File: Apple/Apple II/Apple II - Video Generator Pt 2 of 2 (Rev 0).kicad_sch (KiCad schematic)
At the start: 0 parts

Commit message: Finished Apple II - Sheet 17 - Video Generator Part 2 (Rev 0)
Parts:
- added B11: 74LS08, symbol Apple II:B11_74LS08
- added B12: 74LS11, symbol Apple II:B12_74LS11
- added B13: 74LS02, symbol Apple II:B13_74LS02
- added C11: 74LS04, symbol Apple II:C11_74LS04
- added C14: 74LS32, symbol Apple II:C14_74LS32
- added C2: 47pF, symbol Device:C_Small
- added C3: 5-50pF, symbol Device:C_Variable
- added J324: COMPOSITE VIDEO OUTPUT, symbol Connector:Conn_Coaxial
- added J432: AUX VIDEO CONNECTOR, symbol Connector:Conn_01x04_Male
- added L1: 27µH, symbol Device:L
- added Q?: 2N3904, Package_TO_SOT_THT:TO-92_Inline, symbol Transistor_BJT:2N3904
- added R10: 27Ω, symbol Device:R_US
- added R11: 200Ω, symbol Device:R_Potentiometer_US
- added R5: 1K, symbol Device:R_US
- added R6: 2.7K, symbol Device:R_US
- added R7: 1.5K, symbol Device:R_US
- added R8: 2K, symbol Device:R_US
- added U? (x2): C13_74LS51, symbol Apple II:C13_74LS51
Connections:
- new net: C2.1, C3.1, L1.1, R5.2, R6.1
- new net: Q?.2 (B), R6.2, R7.2, R8.2
- new net: C11.4, U?.1
- new net: B11.8, C14.4, U?.13
- new net: B12.1, B13.1
- new net: J324.1 (In), R10.2
- new net: J432.2 (Pin_2), Q?.1 (E), R11.1
- new net: R10.1, R11.2
- new net +12V: J432.4 (Pin_4)
- new net -5V: J432.3 (Pin_3)
- new net BLANKING: C14.6
- new net COLOR_BURST: B12.12, R5.1
- new net COLOR_REF_{35}: B13.2
- new net Earth: C2.2, C3.2, J324.2 (Ext), J432.1 (Pin_1), L1.2, R11.3
- new net H2: B13.3
- new net H3: U?.10, U?.11, U?.3
- new net H4: B12.2, U?.2
- new net H5: U?.4, U?.5
- new net HBL: B12.13, C14.5, U?.6, U?.9
- new net SYNC_{19}: R8.1, U?.8
- new net V1: C11.3
- new net V2: U?.12
- new net V3: B11.9
- new net V4: B11.10
- new net VIDEO_DATA: R7.1
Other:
- note added: "FROM CLOCK GENERATOR"
- note added: "FROM PART 1"
- note added: "FROM VIDEO ADDRESS GENERATOR"
- note added: "TO MEMORY ADDRESS PT 1"
- note added: "TO PART 1"
- note added: "TO PERIPHREAL I/O"
- title: (none) -> Apple II - Video Generator Part 2

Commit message: Finished Apple II - Sheet 18 - Video Generator Part 2 (Rev 1)
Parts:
- added R9: 10Ω, symbol Device:R_US
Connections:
- net at Q?.3 (C): now also R9.1
- new net +5V: R9.2
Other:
- moved on the sheet: C2, C3, L1, Q?, R10, R11, R5, R6, R7, R8

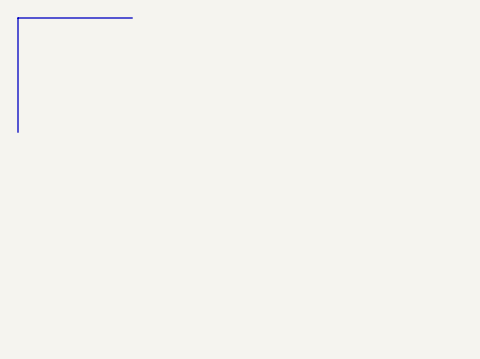
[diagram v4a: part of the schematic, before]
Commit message: Finished Apple II - Sheet 22 - Two-Piece Keyboard
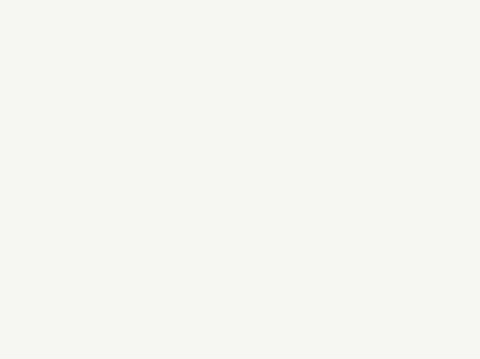
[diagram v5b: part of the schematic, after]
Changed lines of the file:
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@@
-    (stroke (width 0) (type default) (color 0 0 0 0))
-  )
-  (polyline (pts (xy 12.7 0) (xy 0 0))
     (stroke (width 0) (type default) (color 0 0 0 0))
   )
@@
     (stroke (width 0) (type default) (color 0 0 0 0))
   )
-  (polyline (pts (xy 0 0) (xy 0 12.7))
-    (stroke (width 0) (type default) (color 0 0 0 0))
-  )
